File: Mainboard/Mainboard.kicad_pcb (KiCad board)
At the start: 4 copper layers, 31 parts, among them IC1 IP5306, J1 2479774-2, U1 LM3880, U3 TPS22917DBV, U4 TLV62569DBV, U5 TLV75533PDBV, U6 TLV75518PDBV

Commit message: huge update: power/charging, audio, zif connections, screen, cartridge pinout
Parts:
- removed C15: 1uF, Resistor_SMD:R_0603_1608Metric
- removed U5: TLV75533PDBV, Package_TO_SOT_SMD:SOT-23-5
- added C11: .1uF, Capacitor_SMD:C_0603_1608Metric, B.Cu at (152.7, 91.6)
- added C12: 10uF, Capacitor_SMD:C_0603_1608Metric, B.Cu at (151.1, 91.6)
- added C17: 10uF, Capacitor_SMD:C_0603_1608Metric, B.Cu at (134.4, 73.0)
- added C18: 22uF, Capacitor_SMD:C_0603_1608Metric, B.Cu at (134.3, 77.0)
- added JP1: Jumper_3_Open, Jumper:SolderJumper-3_P1.3mm_Open_RoundedPad1.0x1.5mm, F.Cu at (145.9, 87.4)
- added L3: 2.2uH, FPGBA:1206 (metric 2832), F.Cu at (135.1, 76.2)
- added LS1: Speaker, Connector_PinHeader_2.00mm:PinHeader_2x01_P2.00mm_Vertical, F.Cu at (156.4, 93.1)
- added R10: 100k, Resistor_SMD:R_0603_1608Metric, F.Cu at (135.4, 70.0)
- added R8: 1M, Resistor_SMD:R_0603_1608Metric, B.Cu at (148.8, 92.4)
- added R9: 453k, Resistor_SMD:R_0603_1608Metric, B.Cu at (135.8, 77.0)
- added REF**: Hirose_FH12-10S-0.5SH_1x10-1MP_P0.50mm_Horizontal, Connector_FFC-FPC:Hirose_FH12-10S-0.5SH_1x10-1MP_P0.50mm_Horizontal, F.Cu at (153.0, 83.2)
- added REF**: AGB Cart Pin, FPGBA:AGB Cart Pin, F.Cu at (128.0, 92.0)
- added REF**: Hirose_FH12-10S-0.5SH_1x10-1MP_P0.50mm_Horizontal, Connector_FFC-FPC:Hirose_FH12-10S-0.5SH_1x10-1MP_P0.50mm_Horizontal, F.Cu at (101.8, 80.9)
- added REF**: Hirose_FH12-32S-0.5SH_1x32-1MP_P0.50mm_Horizontal, Connector_FFC-FPC:Hirose_FH12-32S-0.5SH_1x32-1MP_P0.50mm_Horizontal, B.Cu at (112.8, 65.5)
- added U2: MAX98357A, Package_DFN_QFN:TQFN-16-1EP_3x3mm_P0.5mm_EP1.23x1.23mm, F.Cu at (149.4, 90.9)
- added U7: TPS62822DLC, Package_SON:Texas_VSON-HR-8_1.5x2mm_P0.5mm, F.Cu at (135.6, 72.8)
- C1, C16, C2, C4, C7, C8, C9, L1, R3, R4, R5, R6, R7, U4, U6: moved to B.Cu
- moved IC1 103.4 mm to (130.7, 71.4)
- moved L2 103.3 mm to (130.7, 77.2)
- moved C10 103.3 mm to (130.1, 80.6)
- moved C1 103.2 mm to (145.1, 71.0)
- moved R3 101.3 mm to (140.6, 76.0), turned to 180 degrees
- moved R2 100.9 mm to (144.3, 75.1), turned to 180 degrees
- moved C5 100.7 mm to (138.3, 72.0), turned to -90 degrees
- moved C8 100.2 mm to (134.3, 67.8)
- moved C9 100.2 mm to (134.3, 70.2)
- moved U1 100.0 mm to (140.8, 74.9)
- moved R1 99.9 mm to (145.7, 73.3)
- moved C6 99.6 mm to (145.0, 71.0)
- moved C14 99.2 mm to (139.6, 80.1), turned to 180 degrees
- moved J1 97.3 mm to (133.8, 61.3)
- moved L1 96.9 mm to (147.9, 76.3), turned to 90 degrees
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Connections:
- REF** pad B6: (no net) -> VREF3V3
- REF** pad D4: (no net) -> VREF3V3
- REF** pad D8: (no net) -> VREF3V3
- REF** pad F17: GND -> (no net)
- REF** pad G3: (no net) -> VREF3V3
- REF** pad H10: (no net) -> /FPGBA_Power/VREF1V8
- REF** pad H9: (no net) -> GND
- REF** pad K13: (no net) -> SPKDIN
- REF** pad K14: (no net) -> SPKBCLK
- REF** pad K16: (no net) -> SPKLRC
- REF** pad L3: (no net) -> VREF3V3
- REF** pad P4: (no net) -> VREF3V3
- REF** pad U5: (no net) -> VREF3V3
- REF** pad V10: (no net) -> VREF3V3
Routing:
- net (no net): track 0.00 -> 1415.5 mm, vias 0 -> 70
- net VREF3V3: track 0.00 -> 55.4 mm, vias 0 -> 17
- net SPKLRC: track 0.00 -> 39.2 mm, vias 0 -> 4
- net SPKDIN: track 0.00 -> 36.9 mm, vias 0 -> 2
- net SPKBCLK: track 0.00 -> 36.9 mm, vias 0 -> 2
- net /FPGBA_Power/VREF5V: track 39.4 -> 13.1 mm
- net GND: track 53.5 -> 72.9 mm, vias 82 -> 86
- net Net-(U7-FB): track 0.00 -> 12.1 mm, vias 0 -> 2
- net /FPGBA Charging/USB5VIN: track 5.01 -> 13.7 mm, vias 0 -> 2
- net Net-(IC1-VOUT): track 2.07 -> 8.50 mm, vias 0 -> 1
- net Net-(U2-OUTP): track 0.00 -> 6.13 mm
- net Net-(U4-FB): track 10.5 -> 4.87 mm
- net Net-(U2-OUTN): track 0.00 -> 5.56 mm
- net Net-(JP1-C): track 0.00 -> 5.49 mm, vias 0 -> 2
- net SYS_5V: track 21.9 -> 16.9 mm, vias 10 -> 9
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- added copper zone on In2.Cu, net /FPGBA Charging/USB5VIN
- added copper zone on B.Cu, net /FPGBA_Power/REF1V
- added copper zone on B.Cu, net /FPGBA_Power/VREF1V8
- added copper zone on F.Cu, net /FPGBA_Power/VREF1V8
- added copper zone on B.Cu, net Net-(U4-SW)
- added copper zone on F.Cu, net Net-(U7-SW)
- added copper zone on B.Cu, net SYS_5V
- added copper zone on B.Cu, net VREF3V3
- added copper zone on F.Cu, net VREF3V3
- added copper zone on In2.Cu, net VREF3V3
- removed copper zone on F.Cu, net /FPGBA_Power/REF1V
- removed copper zone on In2.Cu, net /FPGBA_Power/VREF3V3
- removed copper zone on F.Cu, net Net-(U4-SW)
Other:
- board outline added: 131.2 x 72.3 mm
- board text added: "+12dB"
- board text added: "+3dB"
- board text added: "+9dB"

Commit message: minor updates and graphics silkscreen
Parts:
- added vclk: test, TestPoint:TestPoint_Pad_1.0x1.0mm, F.Cu at (105.5, 64.0)
- C11, C12, R8: moved to F.Cu
- REF** (x2): value Hirose_FH12-10S-0.5SH_1x10-1MP_P0.50mm_Horizontal -> Hirose_FH12-10S-0.5SH
- REF**: value Hirose_FH12-32S-0.5SH_1x32-1MP_P0.50mm_Horizontal -> Hirose_FH12-32S-0.5SH
- moved C12 3.10 mm to (154.2, 91.6)
- moved R8 1.47 mm to (148.8, 93.8)
- moved LS1 0.20 mm to (156.6, 93.1)
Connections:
- REF** pad 10: (no net) -> GND
- REF** pad 8: (no net) -> GND
- REF** pad 9: (no net) -> GND
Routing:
- net (no net): track 1415.5 -> 1379.1 mm, vias 70 -> 66
- net GND: track 72.9 -> 97.2 mm, vias 86 -> 93
- net VREF3V3: track 55.4 -> 56.7 mm
- net Net-(U2-OUTP): track 6.13 -> 6.60 mm, vias 0 -> 2
- net Net-(U2-OUTN): track 5.56 -> 5.92 mm, vias 0 -> 2
- net Net-(U2-~{SD_MODE}): track 2.48 -> 2.19 mm, vias 1 -> 0
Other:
- outline, holes or cut-outs redrawn
- board text added: "FP"
- board text added: "GBA"
- board text added: "rev 1.0"

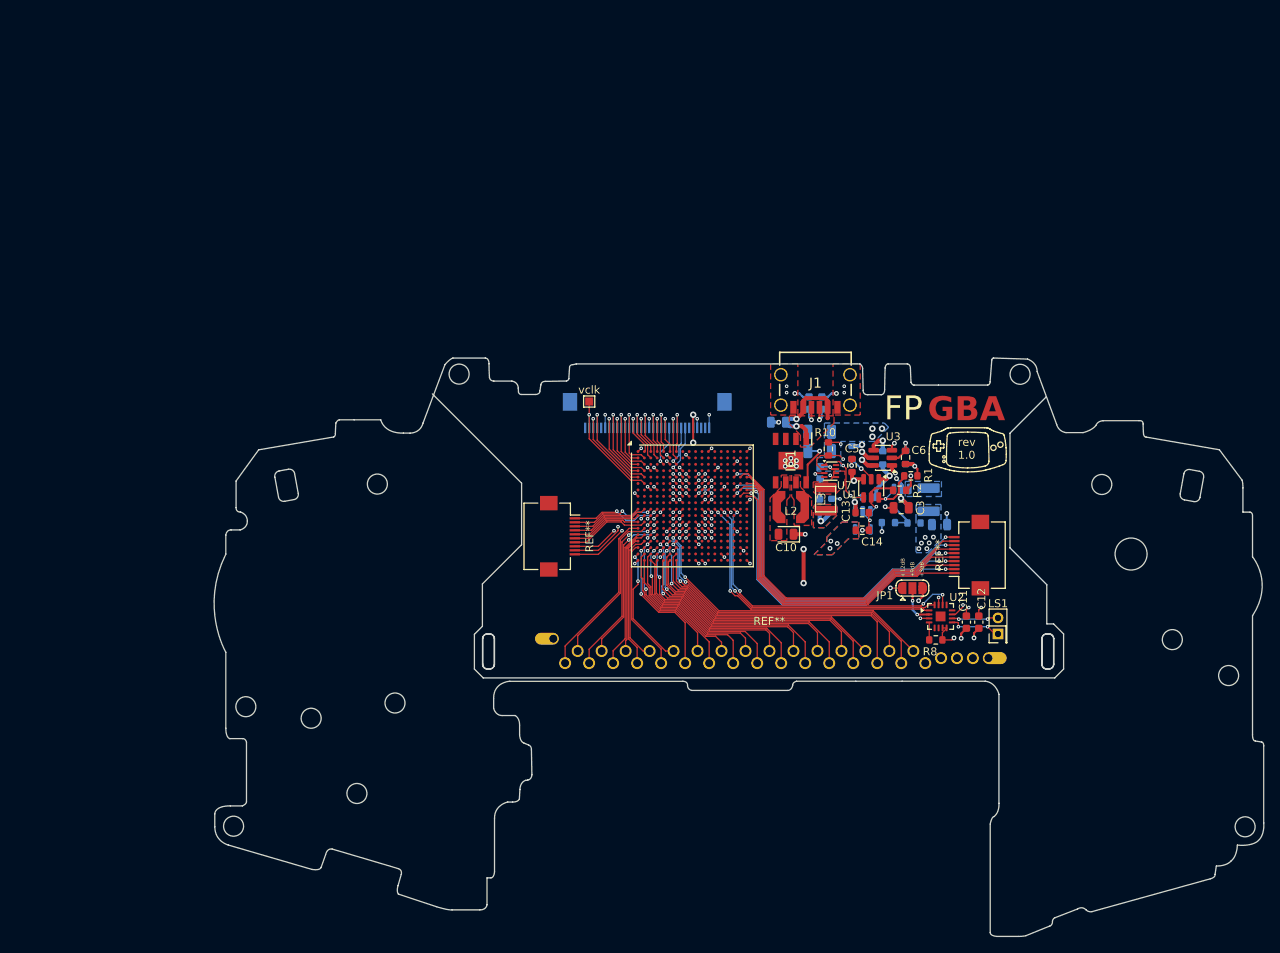
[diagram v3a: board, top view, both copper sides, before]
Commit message: visual updates and imported 3D models
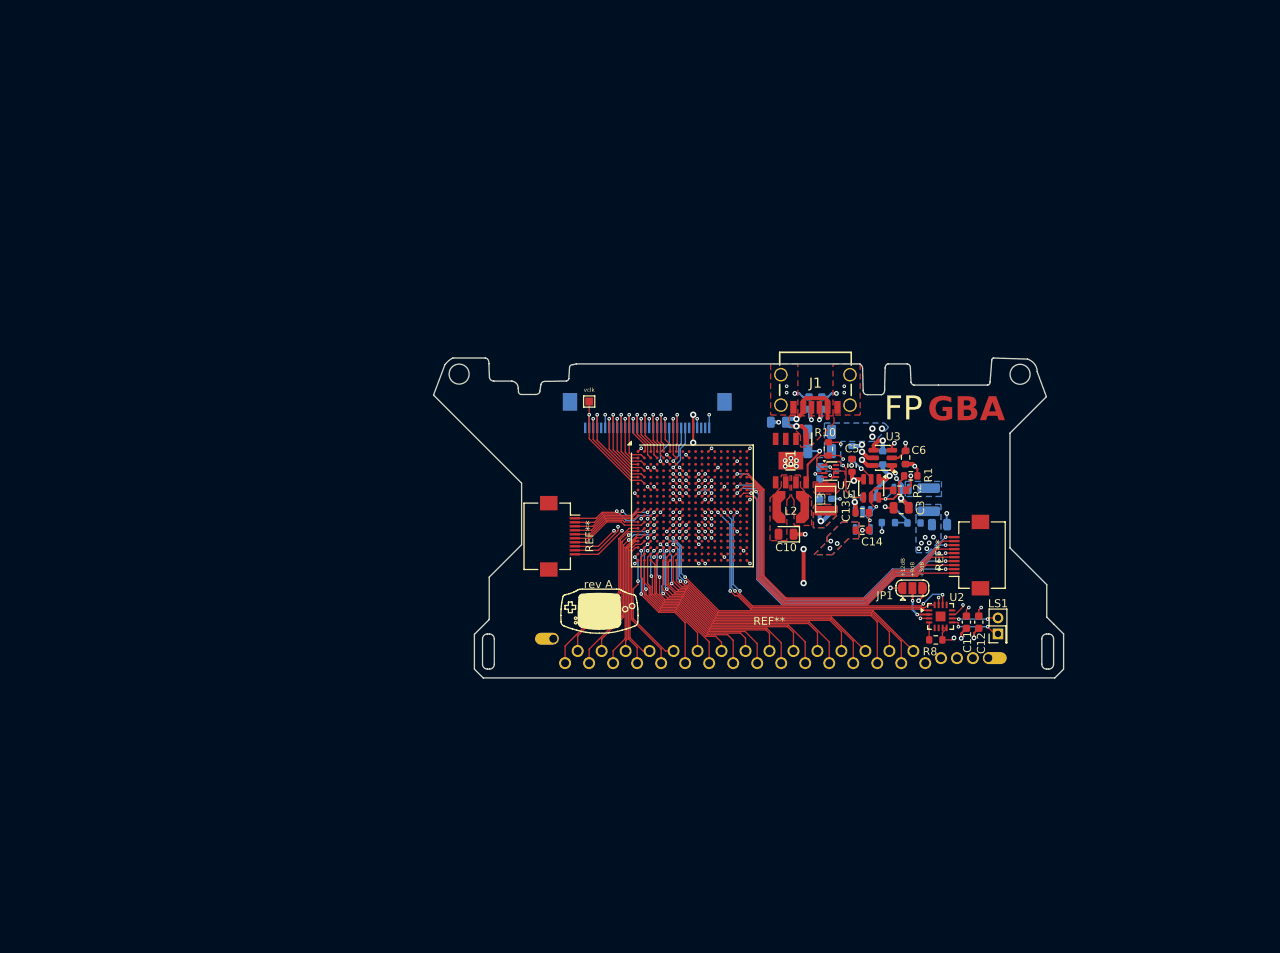
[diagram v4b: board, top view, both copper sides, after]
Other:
- board size 131.2 x 72.3 mm -> 78.8 x 40 mm
- board text added: "rev A"
- board text removed: "rev 1.0"

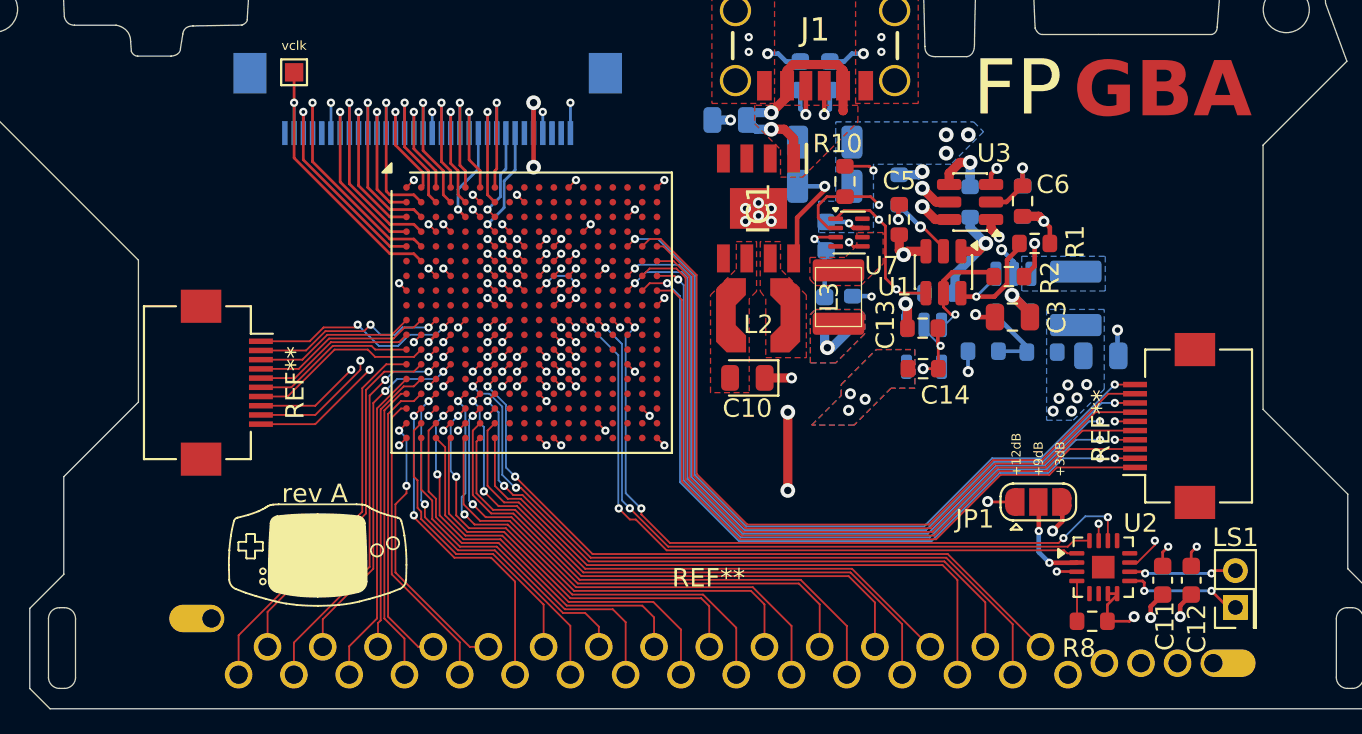
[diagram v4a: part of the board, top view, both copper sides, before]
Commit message: added JTAG + QSPI traces to PCB
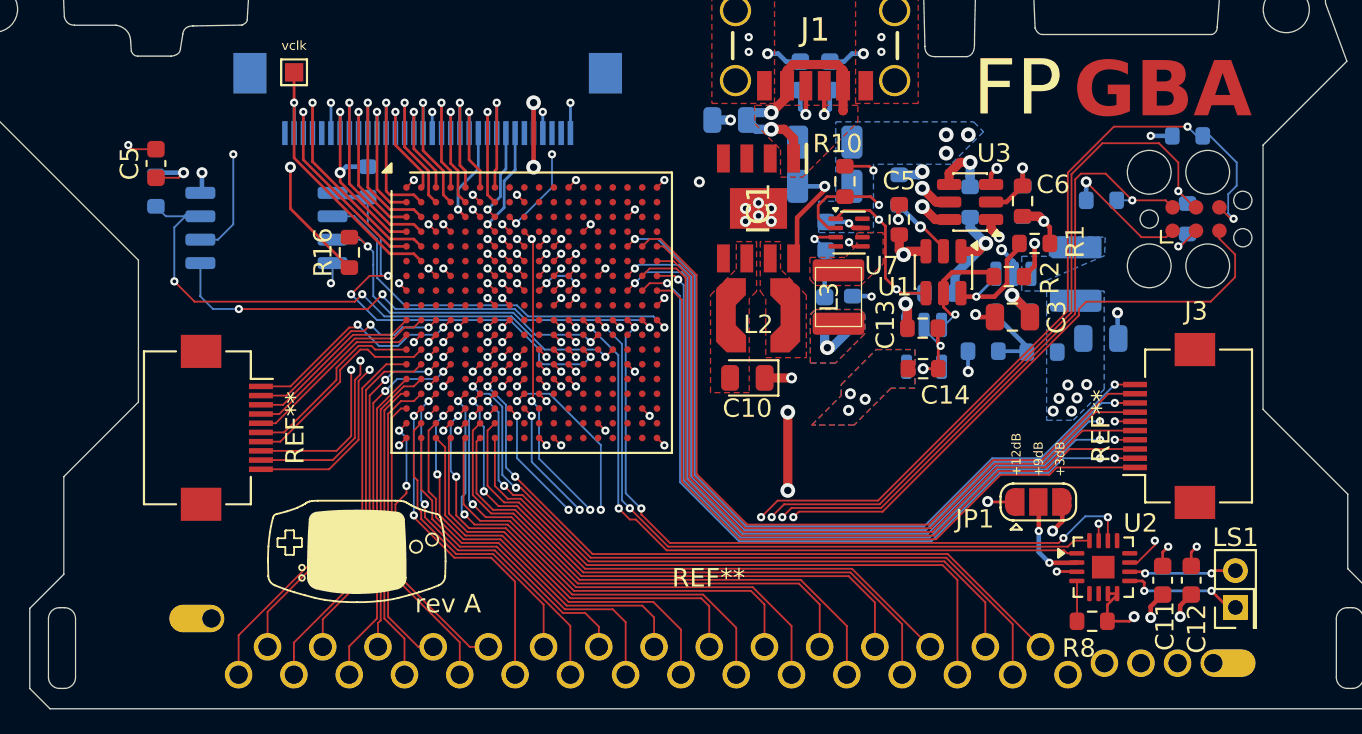
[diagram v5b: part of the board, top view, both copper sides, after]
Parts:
- added C5: 0.1uF, Capacitor_SMD:C_0603_1608Metric, F.Cu at (98.0, 69.0)
- added J3: Conn_01x06_Pin, Connector:Tag-Connect_TC2030-IDC-FP_2x03_P1.27mm_Vertical, F.Cu at (154.5, 72.0)
- added R11: 10k, Resistor_SMD:R_0603_1608Metric, B.Cu at (109.5, 70.0)
- added R12: 10k, Resistor_SMD:R_0603_1608Metric, B.Cu at (98.0, 70.5)
- added R13: 4.7k, Resistor_SMD:R_0603_1608Metric, B.Cu at (149.3, 71.0)
- added R14: 4.7k, Resistor_SMD:R_0603_1608Metric, B.Cu at (154.0, 72.0)
- added R15: 4.7k, Resistor_SMD:R_0603_1608Metric, B.Cu at (154.0, 67.5)
- added R16: 10k, Resistor_SMD:R_0603_1608Metric, F.Cu at (108.5, 73.8)
- added U5: W25Q128JVS, Package_SO:SOIC-8_5.3x5.3mm_P1.27mm, B.Cu at (104.0, 72.5)
- moved REF** 2.45 mm to (101.8, 83.3)
- moved L1 1.32 mm to (147.9, 75.0)
- moved C4 0.94 mm to (149.3, 78.5)
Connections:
- REF** pad C8: (no net) -> CCLK_0
- REF** pad D9: (no net) -> TCK_0
- REF** pad K17: (no net) -> D00_MOSI
- REF** pad K18: (no net) -> D01
- REF** pad L14: (no net) -> D02
- REF** pad M13: (no net) -> FCS_B
- REF** pad M15: (no net) -> D03
- REF** pad R9: (no net) -> TDI_0
- REF** pad T8: (no net) -> TDO_0
- REF** pad T9: (no net) -> TMS_0
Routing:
- net TCK_0: track 0.00 -> 66.1 mm, vias 0 -> 5
- net TDI_0: track 0.00 -> 63.2 mm, vias 0 -> 5
- net VREF3V3: track 56.7 -> 116.5 mm, vias 17 -> 25
- net TMS_0: track 0.00 -> 53.2 mm, vias 0 -> 4
- net TDO_0: track 0.00 -> 52.3 mm, vias 0 -> 3
- net D03: track 0.00 -> 33.2 mm, vias 0 -> 3
- net CCLK_0: track 0.00 -> 28.4 mm, vias 0 -> 3
- net D00_MOSI: track 0.00 -> 28.2 mm, vias 0 -> 3
- net FCS_B: track 0.00 -> 25.0 mm, vias 0 -> 3
- net D01: track 0.00 -> 22.3 mm, vias 0 -> 1
- net D02: track 0.00 -> 19.5 mm, vias 0 -> 2
- net GND: track 97.2 -> 111.1 mm, vias 93 -> 96
- net (no net): track 1379.1 -> 1377.3 mm, vias 66 -> 65

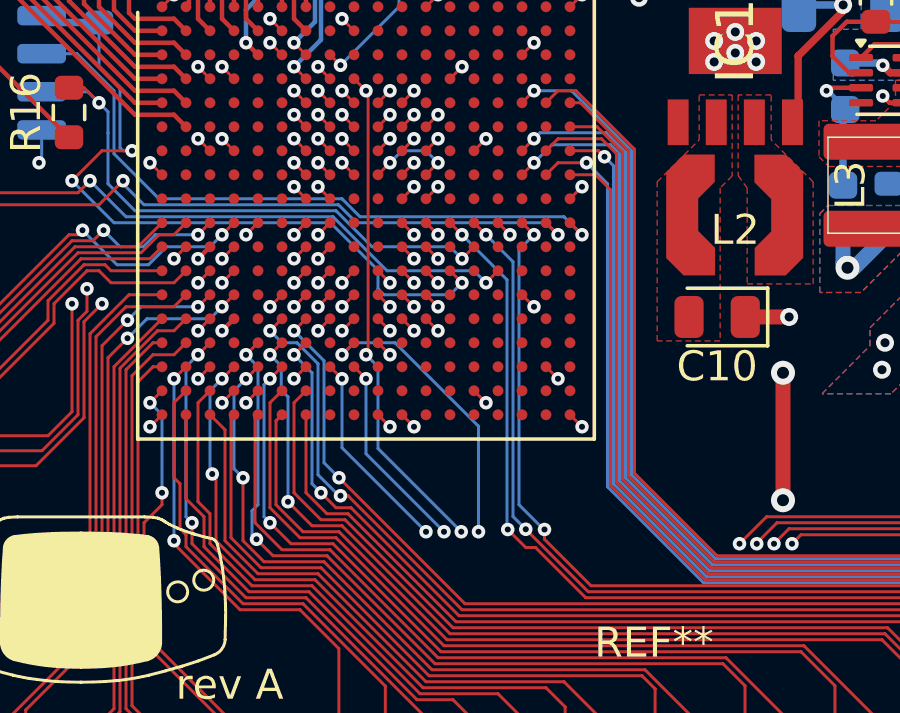
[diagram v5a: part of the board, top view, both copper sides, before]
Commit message: pinout updates
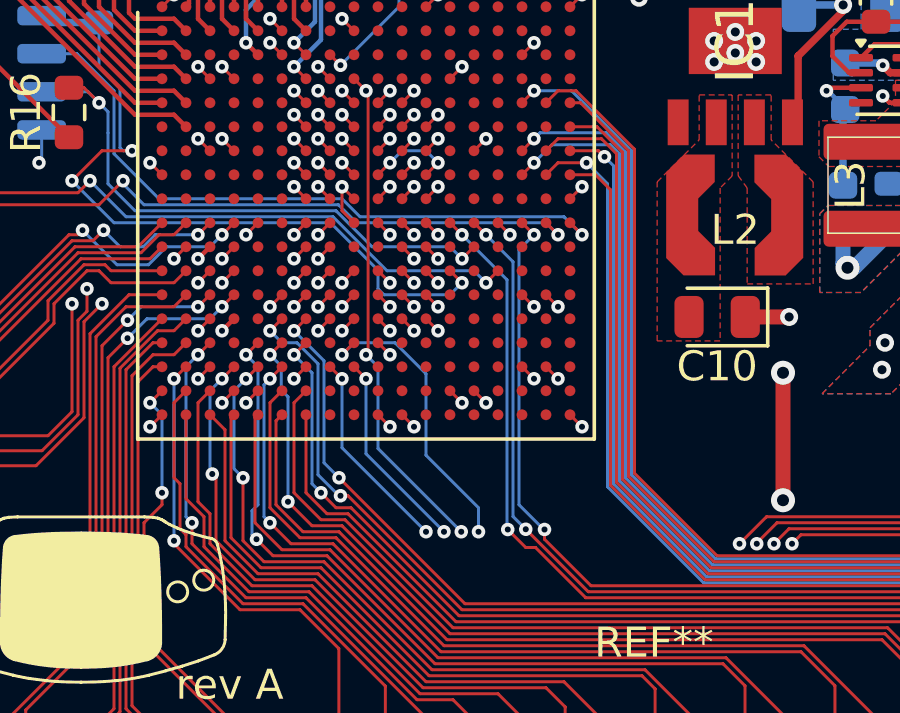
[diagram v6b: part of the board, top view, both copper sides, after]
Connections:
- REF** pad K9: (no net) -> GND
- REF** pad N17: (no net) -> VREF3V3
- REF** pad T16: (no net) -> VREF3V3
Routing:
- net VREF3V3: track 116.5 -> 120.9 mm, vias 25 -> 28
- net GND: track 111.1 -> 114.2 mm, vias 96 -> 99
